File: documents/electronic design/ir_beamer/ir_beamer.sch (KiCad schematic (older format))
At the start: 20 parts, among them U1 74HC595D, U2 STM32F103HEADER, U3 74HC595D, U4 SE8R01_module

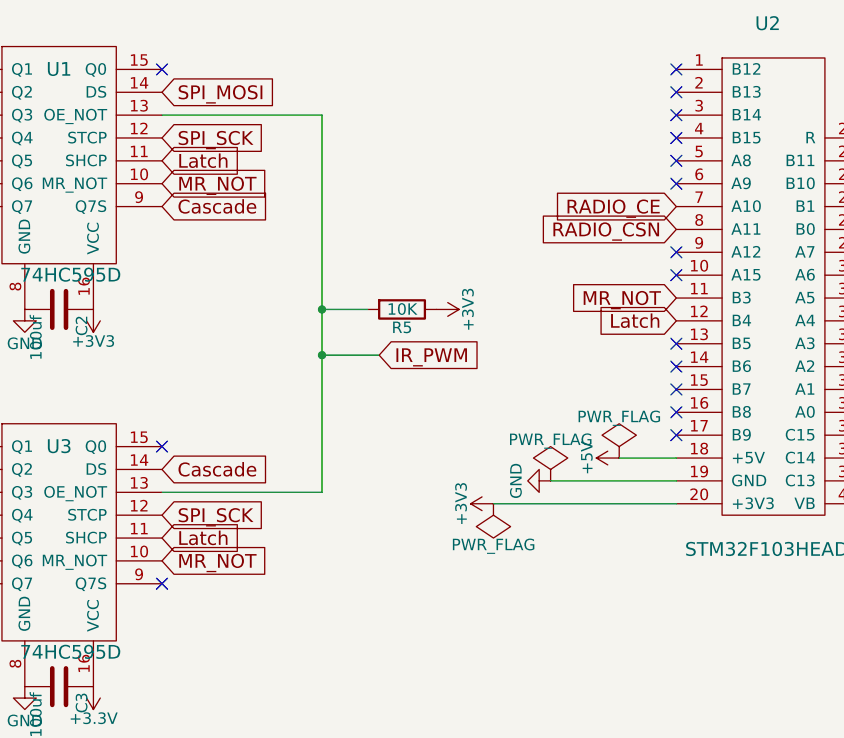
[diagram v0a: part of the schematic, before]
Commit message: update beamere pcb - MR_TOT in shift register, pull down
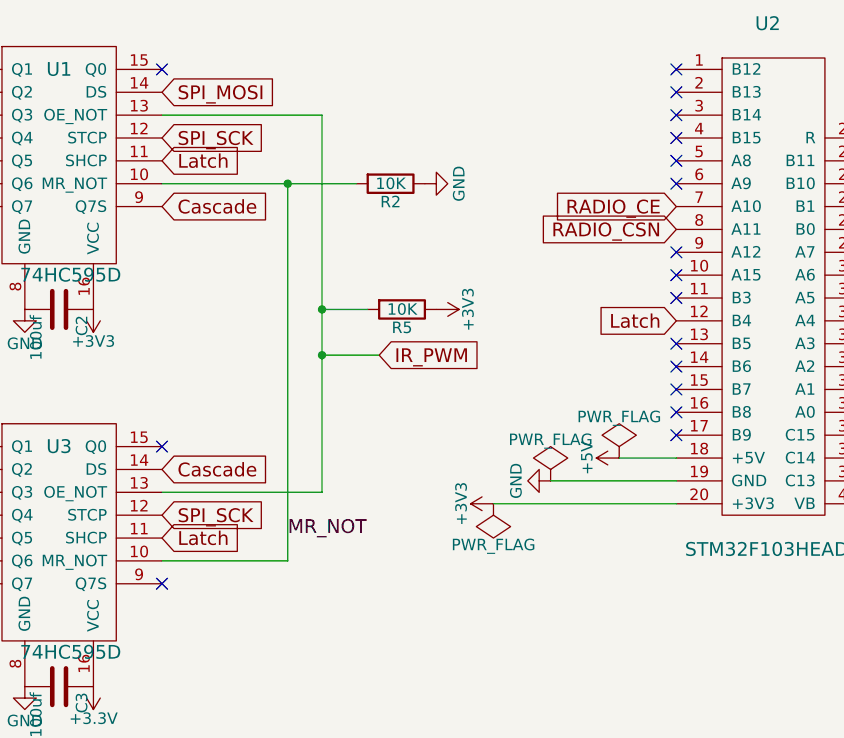
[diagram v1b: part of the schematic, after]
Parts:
- added R2: 10K, Capacitors_SMD:C_0805_HandSoldering, symbol R
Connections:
- net GND: now also R2.1
- net MR_NOT: now also R2.2; no longer U2.11 (B3)
- no-connect marks 31 -> 32
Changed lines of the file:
@@
 Text GLabel 1200 7150 0    60   Input ~ 0
 IR_GND
-Text GLabel 4700 2900 2    60   Input ~ 0
-MR_NOT
-Text GLabel 4700 1250 2    60   Input ~ 0
-MR_NOT
-Text GLabel 6950 1750 0    60   Input ~ 0
-MR_NOT
 Wire Wire Line
 	5400 2600 4700 2600
@@
 NoConn ~ 7800 1350
 NoConn ~ 7800 1850
+$Comp
+L GND #PWR015
+U 1 1 57BA1E9B
+P 5850 1250
+F 0 "#PWR015" H 5850 1000 50  0001 C CNN
+F 1 "GND" H 5850 1100 50  0000 C CNN
+F 2 "" H 5850 1250 50  0000 C CNN
+F 3 "" H 5850 1250 50  0000 C CNN
+	1    5850 1250
+	0    -1   -1   0
+$EndComp
+Wire Wire Line
+	4700 1250 5550 1250
+Wire Wire Line
+	5250 1250 5250 2900
+Wire Wire Line
+	5250 2900 4700 2900
+$Comp
+L R R2
+U 1 1 57BA1F05
+P 5700 1250
+F 0 "R2" V 5780 1250 50  0000 C CNN
+F 1 "10K" V 5700 1250 50  0000 C CNN
+F 2 "Capacitors_SMD:C_0805_HandSoldering" V 5630 1250 50  0001 C CNN
+F 3 "" H 5700 1250 50  0000 C CNN
+	1    5700 1250
+	0    1    1    0
+$EndComp
+Connection ~ 5250 1250
+NoConn ~ 6950 1750
+Text Label 5250 2800 0    60   ~ 0
+MR_NOT
 $EndSCHEMATC

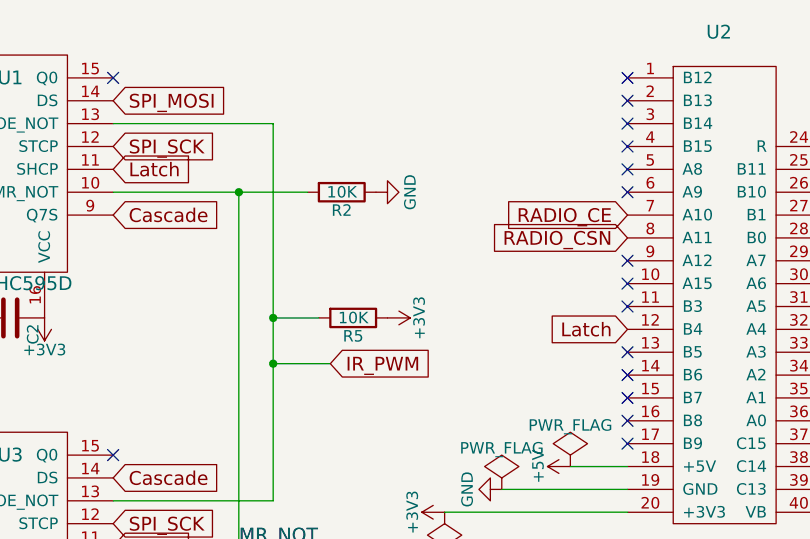
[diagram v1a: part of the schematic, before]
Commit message: fix mistake with pull up/ and down resistors in beamer pcb
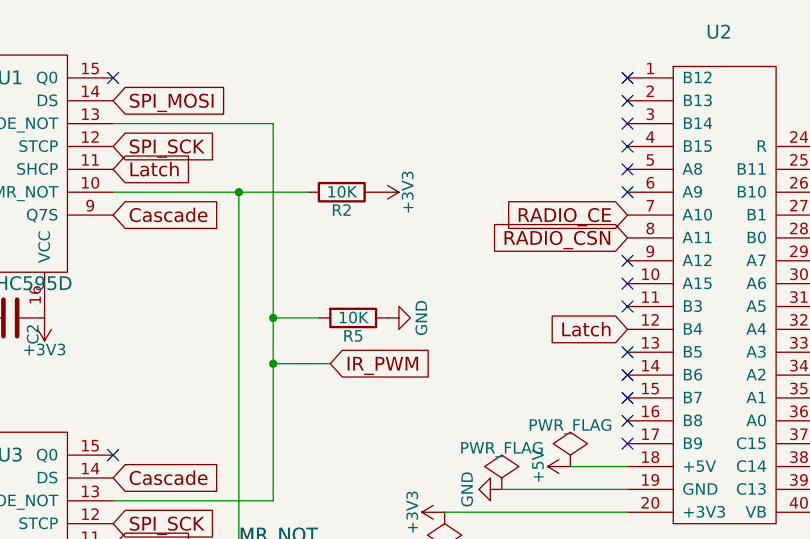
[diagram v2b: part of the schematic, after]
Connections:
- net +3V3: now also R2.1; no longer R5.1
- net GND: now also R5.1; no longer R2.1
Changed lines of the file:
@@
 L +3V3 #PWR010
 U 1 1 57A116F2
-P 5900 1800
-F 0 "#PWR010" H 5900 1650 50  0001 C CNN
-F 1 "+3V3" H 5900 1940 50  0000 C CNN
-F 2 "" H 5900 1800 50  0000 C CNN
-F 3 "" H 5900 1800 50  0000 C CNN
-	1    5900 1800
+P 5850 1250
+F 0 "#PWR010" H 5850 1100 50  0001 C CNN
+F 1 "+3V3" H 5850 1390 50  0000 C CNN
+F 2 "" H 5850 1250 50  0000 C CNN
+F 3 "" H 5850 1250 50  0000 C CNN
+	1    5850 1250
 	0    1    1    0
 $EndComp
@@
 L GND #PWR015
 U 1 1 57BA1E9B
-P 5850 1250
-F 0 "#PWR015" H 5850 1000 50  0001 C CNN
-F 1 "GND" H 5850 1100 50  0000 C CNN
-F 2 "" H 5850 1250 50  0000 C CNN
-F 3 "" H 5850 1250 50  0000 C CNN
-	1    5850 1250
+P 5900 1800
+F 0 "#PWR015" H 5900 1550 50  0001 C CNN
+F 1 "GND" H 5900 1650 50  0000 C CNN
+F 2 "" H 5900 1800 50  0000 C CNN
+F 3 "" H 5900 1800 50  0000 C CNN
+	1    5900 1800
 	0    -1   -1   0
 $EndComp

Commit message: update pcb
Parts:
- C1: value 100uf -> 100nf; footprint Capacitors_SMD:C_1206_HandSoldering -> Capacitors_SMD:C_0603_HandSoldering
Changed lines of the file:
@@
-$EndComp
-$Comp
-L C C1
-U 1 1 57B95404
-P 4250 4650
-F 0 "C1" H 4275 4750 50  0000 L CNN
-F 1 "100uf" H 4275 4550 50  0000 L CNN
-F 2 "Capacitors_SMD:C_1206_HandSoldering" H 4288 4500 50  0001 C CNN
-F 3 "" H 4250 4650 50  0000 C CNN
-	1    4250 4650
-	0    1    1    0
 $EndComp
 $Comp
@@
 Text Label 5250 2800 0    60   ~ 0
 MR_NOT
+$Comp
+L C C1
+U 1 1 57BCA083
+P 4250 4650
+F 0 "C1" H 4275 4750 50  0000 L CNN
+F 1 "100nf" H 4275 4550 50  0000 L CNN
+F 2 "Capacitors_SMD:C_0603_HandSoldering" H 4288 4500 50  0001 C CNN
+F 3 "" H 4250 4650 50  0000 C CNN
+	1    4250 4650
+	0    1    1    0
+$EndComp
 $EndSCHEMATC

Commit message: update pcb for beamer
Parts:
- removed U2: STM32F103HEADER, footprints:STM32F103_header_footprint, symbol STM32F103HEADER
- added P1: CONN_02X05, Pin_Headers:Pin_Header_Straight_2x05, symbol CONN_02X05
- C1: value 100nf -> 100uf
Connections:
- net +3V3: now also P1.9 (P9)
- net GND: now also P1.7 (P7)
- net IR_LED_1: now also U3.3 (Q3); no longer U3.1 (Q1)
- net IR_LED_10: now also U3.6 (Q6); no longer U3.4 (Q4)
- net IR_LED_2: now also U1.3 (Q3); no longer U1.2 (Q2)
- net IR_LED_3: now also U1.4 (Q4); no longer U1.3 (Q3)
- net IR_LED_4: now also U1.5 (Q5); no longer U1.4 (Q4)
- net IR_LED_5: now also U1.6 (Q6); no longer U1.5 (Q5)
- net IR_LED_6: now also U1.7 (Q7); no longer U1.6 (Q6)
- net IR_LED_7: now also U3.2 (Q2); no longer U1.7 (Q7)
- net IR_LED_8: now also U3.4 (Q4); no longer U3.2 (Q2)
- net IR_LED_9: now also U3.5 (Q5); no longer U3.3 (Q3)
- net IR_LED_DATA: now also U3.1 (Q1); no longer U3.7 (Q7)
- net IR_PWM: now also P1.10 (P10)
- net Latch: now also P1.5 (P5)
- net RADIO_CE: now also P1.1 (P1)
- net RADIO_CSN: now also P1.3 (P3)
- net RADIO_IRQ: now also P1.2 (P2)
- net SPI_MISO: now also P1.6 (P6)
- net SPI_MOSI: now also P1.4 (P4)
- net SPI_SCK: now also P1.8 (P8)
- no-connect marks 32 -> 9
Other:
- note added: "A5 ------> SPI1_SCK\nA6 ------> SPI1_MISO\nA7 ------> SPI1_MOSI \n\nA0 ------> IR_PWM (TIM2 CH1 PWM out)\n\nA10 -> CE\nA11 -> CSN\nB0 -> IRQ\nB4 -> Latch\n"
- note removed: "A5 ------> SPI1_SCK\nA6 ------> SPI1_MISO\nA7 ------> SPI1_MOSI \n\nA0 ------> IR_PWM (TIM2 CH1 PWM out)\n\nA10 -> CE\nA11 -> CSN\nB0 -> IRQ\n"
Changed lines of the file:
@@
 Comment4 ""
 $EndDescr
-NoConn ~ 6950 750
-NoConn ~ 6950 850
-NoConn ~ 6950 950
-NoConn ~ 6950 1050
-NoConn ~ 6950 1150
-NoConn ~ 6950 1550
-NoConn ~ 6950 1950
-NoConn ~ 6950 2050
-NoConn ~ 6950 2150
-NoConn ~ 6950 2250
-NoConn ~ 6950 2350
-NoConn ~ 7800 2650
-NoConn ~ 7800 2550
-NoConn ~ 7800 2450
-NoConn ~ 7800 2350
-NoConn ~ 7800 2150
-NoConn ~ 7800 1250
-NoConn ~ 7800 1150
-NoConn ~ 7800 1050
 $Comp
 L LED D2
@@
 $EndComp
 Text Notes 8800 1650 0    60   ~ 0
-A5     ------> SPI1_SCK\nA6     ------> SPI1_MISO\nA7     ------> SPI1_MOSI \n\nA0     ------> IR_PWM (TIM2 CH1 PWM out)\n\nA10 -> CE\nA11 -> CSN\nB0  -> IRQ\n
-Text GLabel 7800 1750 2    60   Input ~ 0
+A5     ------> SPI1_SCK\nA6     ------> SPI1_MISO\nA7     ------> SPI1_MOSI \n\nA0     ------> IR_PWM (TIM2 CH1 PWM out)\n\nA10 -> CE\nA11 -> CSN\nB0  -> IRQ\nB4  -> Latch\n
+Text GLabel 7700 1150 2    60   Input ~ 0
 SPI_SCK
-Text GLabel 7800 1550 2    60   Input ~ 0
+Text GLabel 7700 950  2    60   Input ~ 0
 SPI_MOSI
 Text GLabel 4700 1050 2    60   Input ~ 0
@@
 Text GLabel 4700 850  2    60   Input ~ 0
 SPI_MOSI
-NoConn ~ 6950 1250
-Text GLabel 3800 2400 0    60   Input ~ 0
+Text GLabel 3800 2600 0    60   Input ~ 0
 IR_LED_1
-Text GLabel 3800 850  0    60   Input ~ 0
+Text GLabel 3800 950  0    60   Input ~ 0
 IR_LED_2
-Text GLabel 3800 950  0    60   Input ~ 0
+Text GLabel 3800 1050 0    60   Input ~ 0
 IR_LED_3
-Text GLabel 3800 1050 0    60   Input ~ 0
+Text GLabel 3800 1150 0    60   Input ~ 0
 IR_LED_4
-Text GLabel 3800 1150 0    60   Input ~ 0
+Text GLabel 3800 1250 0    60   Input ~ 0
 IR_LED_5
-Text GLabel 3800 1250 0    60   Input ~ 0
+Text GLabel 3800 1350 0    60   Input ~ 0
 IR_LED_6
-Text GLabel 3800 1350 0    60   Input ~ 0
+Text GLabel 3800 2500 0    60   Input ~ 0
 IR_LED_7
-Text GLabel 7800 2250 2    60   Input ~ 0
+Text GLabel 7700 1250 2    60   Input ~ 0
 IR_PWM
 $Comp
@@
 	1    0    0    -1
 $EndComp
-Text GLabel 3800 2500 0    60   Input ~ 0
+Text GLabel 3800 2700 0    60   Input ~ 0
 IR_LED_8
-Text GLabel 3800 2600 0    60   Input ~ 0
+Text GLabel 3800 2800 0    60   Input ~ 0
 IR_LED_9
-Text GLabel 3800 2700 0    60   Input ~ 0
+Text GLabel 3800 2900 0    60   Input ~ 0
 IR_LED_10
-NoConn ~ 3800 2800
-NoConn ~ 3800 2900
 $Comp
 L 74HC595D U1
@@
 	1    0    0    -1
 $EndComp
-NoConn ~ 7800 2050
-Text GLabel 6950 1850 0    60   Input ~ 0
+Text GLabel 7200 1050 0    60   Input ~ 0
 Latch
 $Comp
 L +3V3 #PWR03
 U 1 1 578F2608
-P 6150 2650
-F 0 "#PWR03" H 6150 2500 50  0001 C CNN
-F 1 "+3V3" H 6150 2790 50  0000 C CNN
-F 2 "" H 6150 2650 50  0000 C CNN
-F 3 "" H 6150 2650 50  0000 C CNN
-	1    6150 2650
+P 6400 1250
+F 0 "#PWR03" H 6400 1100 50  0001 C CNN
+F 1 "+3V3" H 6400 1390 50  0000 C CNN
+F 2 "" H 6400 1250 50  0000 C CNN
+F 3 "" H 6400 1250 50  0000 C CNN
+	1    6400 1250
 	0    -1   -1   0
 $EndComp
@@
 L PWR_FLAG #FLG04
 U 1 1 578F2694
-P 6400 2550
-F 0 "#FLG04" H 6400 2645 50  0001 C CNN
-F 1 "PWR_FLAG" H 6400 2730 50  0000 C CNN
-F 2 "" H 6400 2550 50  0000 C CNN
-F 3 "" H 6400 2550 50  0000 C CNN
-	1    6400 2550
+P 6650 1150
+F 0 "#FLG04" H 6650 1245 50  0001 C CNN
+F 1 "PWR_FLAG" H 6650 1330 50  0000 C CNN
+F 2 "" H 6650 1150 50  0000 C CNN
+F 3 "" H 6650 1150 50  0000 C CNN
+	1    6650 1150
 	1    0    0    -1
 $EndComp
@@
 L GND #PWR05
 U 1 1 5787C14A
-P 6400 2550
-F 0 "#PWR05" H 6400 2300 50  0001 C CNN
-F 1 "GND" H 6400 2400 50  0000 C CNN
-F 2 "" H 6400 2550 50  0000 C CNN
-F 3 "" H 6400 2550 50  0000 C CNN
-	1    6400 2550
+P 6650 1150
+F 0 "#PWR05" H 6650 900 50  0001 C CNN
+F 1 "GND" H 6650 1000 50  0000 C CNN
+F 2 "" H 6650 1150 50  0000 C CNN
+F 3 "" H 6650 1150 50  0000 C CNN
+	1    6650 1150
 	0    1    1    0
 $EndComp
@@
 L PWR_FLAG #FLG06
 U 1 1 578F289B
-P 6150 2650
-F 0 "#FLG06" H 6150 2745 50  0001 C CNN
-F 1 "PWR_FLAG" H 6150 2830 50  0000 C CNN
-F 2 "" H 6150 2650 50  0000 C CNN
-F 3 "" H 6150 2650 50  0000 C CNN
-	1    6150 2650
+P 6400 1250
+F 0 "#FLG06" H 6400 1345 50  0001 C CNN
+F 1 "PWR_FLAG" H 6400 1430 50  0000 C CNN
+F 2 "" H 6400 1250 50  0000 C CNN
+F 3 "" H 6400 1250 50  0000 C CNN
+	1    6400 1250
 	-1   0    0    1
-$EndComp
-$Comp
-L STM32F103HEADER U2
-U 1 1 578F444B
-P 7200 1800
-F 0 "U2" H 7350 3050 60  0000 C CNN
-F 1 "STM32F103HEADER" H 7400 750 60  0000 C CNN
-F 2 "footprints:STM32F103_header_footprint" H 6550 2800 60  0001 C CNN
-F 3 "" H 6550 2800 60  0000 C CNN
-	1    7200 1800
-	1    0    0    -1
 $EndComp
 $Comp
@@
 	-1   0    0    1
 $EndComp
-NoConn ~ 7800 1950
 Text GLabel 4700 2800 2    60   Input ~ 0
 Latch
 Text GLabel 4700 1150 2    60   Input ~ 0
 Latch
-$Comp
-L +5V #PWR08
-U 1 1 57910C6F
-P 6700 2450
-F 0 "#PWR08" H 6700 2300 50  0001 C CNN
-F 1 "+5V" H 6700 2590 50  0000 C CNN
-F 2 "" H 6700 2450 50  0000 C CNN
-F 3 "" H 6700 2450 50  0000 C CNN
-	1    6700 2450
-	0    -1   -1   0
-$EndComp
-$Comp
-L PWR_FLAG #FLG09
-U 1 1 57910CFC
-P 6700 2450
-F 0 "#FLG09" H 6700 2545 50  0001 C CNN
-F 1 "PWR_FLAG" H 6700 2630 50  0000 C CNN
-F 2 "" H 6700 2450 50  0000 C CNN
-F 3 "" H 6700 2450 50  0000 C CNN
-	1    6700 2450
-	1    0    0    -1
-$EndComp
 Text GLabel 4700 1350 2    60   Input ~ 0
 Cascade
@@
 IR_PWM
 $Comp
-L +3V3 #PWR010
+L +3V3 #PWR08
 U 1 1 57A116F2
 P 5850 1250
-F 0 "#PWR010" H 5850 1100 50  0001 C CNN
+F 0 "#PWR08" H 5850 1100 50  0001 C CNN
 F 1 "+3V3" H 5850 1390 50  0000 C CNN
 F 2 "" H 5850 1250 50  0000 C CNN
@@
 Text GLabel 1500 700  2    60   Input ~ 0
 IR_GND
-Text GLabel 3800 3000 0    60   Input ~ 0
+Text GLabel 3800 2400 0    60   Input ~ 0
 IR_LED_DATA
 NoConn ~ 4700 3000
@@
 NoConn ~ 4700 750
 $Comp
-L GND #PWR011
+L GND #PWR09
 U 1 1 5787C121
 P 4100 1800
-F 0 "#PWR011" H 4100 1550 50  0001 C CNN
+F 0 "#PWR09" H 4100 1550 50  0001 C CNN
 F 1 "GND" H 4100 1650 50  0000 C CNN
 F 2 "" H 4100 1800 50  0000 C CNN
@@
 	5400 950  4700 950
 Wire Wire Line
-	6950 2650 6150 2650
-Wire Wire Line
-	6400 2550 6950 2550
-Wire Wire Line
-	6950 2450 6700 2450
+	7200 1250 6400 1250
+Wire Wire Line
+	6650 1150 7200 1150
 NoConn ~ 3800 750
 $Comp
-L GND #PWR012
+L GND #PWR010
 U 1 1 57AB0120
 P 1200 700
-F 0 "#PWR012" H 1200 450 50  0001 C CNN
+F 0 "#PWR010" H 1200 450 50  0001 C CNN
 F 1 "GND" H 1200 550 50  0000 C CNN
 F 2 "" H 1200 700 50  0000 C CNN
@@
 RADIO_CE
 $Comp
-L GND #PWR013
+L GND #PWR011
 U 1 1 57B954EB
 P 4400 4950
-F 0 "#PWR013" H 4400 4700 50  0001 C CNN
+F 0 "#PWR011" H 4400 4700 50  0001 C CNN
 F 1 "GND" H 4400 4800 50  0000 C CNN
 F 2 "" H 4400 4950 50  0000 C CNN
@@
 $EndComp
 $Comp
-L +3.3V #PWR014
+L +3.3V #PWR012
 U 1 1 57B95532
 P 4100 4950
-F 0 "#PWR014" H 4100 4800 50  0001 C CNN
+F 0 "#PWR012" H 4100 4800 50  0001 C CNN
 F 1 "+3.3V" H 4100 5090 50  0000 C CNN
 F 2 "" H 4100 4950 50  0000 C CNN
@@
 	1    4100 4950
 	-1   0    0    1
+$EndComp
+$Comp
+L C C1
+U 1 1 57B95404
+P 4250 4650
+F 0 "C1" H 4275 4750 50  0000 L CNN
+F 1 "100uf" H 4275 4550 50  0000 L CNN
+F 2 "Capacitors_SMD:C_0603_HandSoldering" H 4288 4500 50  0001 C CNN
+F 3 "" H 4250 4650 50  0000 C CNN
+	1    4250 4650
+	0    1    1    0
 $EndComp
 $Comp
@@
 Wire Wire Line
 	4400 4950 4400 4650
-Text GLabel 6950 1350 0    60   Input ~ 0
+Text GLabel 7200 850  0    60   Input ~ 0
 RADIO_CE
-Text GLabel 6950 1450 0    60   Input ~ 0
+Text GLabel 7200 950  0    60   Input ~ 0
 RADIO_CSN
-Text GLabel 7800 1450 2    60   Input ~ 0
+Text GLabel 7700 850  2    60   Input ~ 0
 RADIO_IRQ
-Text GLabel 7800 1650 2    60   Input ~ 0
+Text GLabel 7700 1050 2    60   Input ~ 0
 SPI_MISO
 Text GLabel 4650 4100 2    60   Input ~ 0
 SPI_MISO
-NoConn ~ 6950 1650
-NoConn ~ 7800 1350
-NoConn ~ 7800 1850
-$Comp
-L GND #PWR015
+$Comp
+L GND #PWR013
 U 1 1 57BA1E9B
 P 5900 1800
-F 0 "#PWR015" H 5900 1550 50  0001 C CNN
+F 0 "#PWR013" H 5900 1550 50  0001 C CNN
 F 1 "GND" H 5900 1650 50  0000 C CNN
 F 2 "" H 5900 1800 50  0000 C CNN
@@
 $EndComp
 Connection ~ 5250 1250
-NoConn ~ 6950 1750
 Text Label 5250 2800 0    60   ~ 0
 MR_NOT
-$Comp
-L C C1
-U 1 1 57BCA083
-P 4250 4650
-F 0 "C1" H 4275 4750 50  0000 L CNN
-F 1 "100nf" H 4275 4550 50  0000 L CNN
-F 2 "Capacitors_SMD:C_0603_HandSoldering" H 4288 4500 50  0001 C CNN
-F 3 "" H 4250 4650 50  0000 C CNN
-	1    4250 4650
-	0    1    1    0
+NoConn ~ 3800 3000
+NoConn ~ 5500 3650
+NoConn ~ 900  6150
+NoConn ~ 3800 850
+NoConn ~ 3400 3950
+$Comp
+L CONN_02X05 P1
+U 1 1 57C5E47E
+P 7450 1050
+F 0 "P1" H 7450 1350 50  0000 C CNN
+F 1 "CONN_02X05" H 7450 750 50  0000 C CNN
+F 2 "Pin_Headers:Pin_Header_Straight_2x05" H 7450 -150 50  0001 C CNN
+F 3 "" H 7450 -150 50  0000 C CNN
+	1    7450 1050
+	1    0    0    -1
 $EndComp
 $EndSCHEMATC
